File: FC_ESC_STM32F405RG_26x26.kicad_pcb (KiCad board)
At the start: 2 copper layers, 34 x 34 mm, 225 parts, among them J1 Conn_02x02_Odd_Even, J10 UART4, J11 PWM, J12 Conn_02x02_Odd_Even, J13 ALARM, J14 LED_STRIP, J15 RC, J16 MOTOR, J17 MOTOR, J18 MOTOR, J19 MOTOR, J2 ESC_PROG, J20 USB_A, J21 Conn_02x03_Odd_Even, J22 Conn_02x02_Odd_Even, J3 Debugger, J4 VOL_CUR, J5 RSSI, J6 I2C2_UART3, J7 SD CARD, J8 UART1, J9 UART6, Q1 SIZ200, Q10 SIZ200, Q11 SIZ200, Q12 SIZ200, Q2 SIZ200, Q3 SIZ200, Q4 SIZ200, Q5 SIZ200, Q6 SIZ200, Q7 SIZ200, Q8 SIZ200, Q9 SIZ200, U1 EFM8BB21, U10 FD6288Q, U11 outline, U12 MPU-6000, U13 BMP280, U15 STM32F405RGTx, U16 TPS54331D, U2 EFM8BB21, U3 TPS54560BDDA, U4 FD6288Q, U5 FD6288Q, U6 AT7456, U7 EFM8BB21, U8 EFM8BB21, U9 FD6288Q, Y1 8MHz, Y2 8Mhz

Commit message: update placement
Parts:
- removed J1, J22: Conn_02x02_Odd_Even, Proj_footprint:PinHeader_2x02_P1.27mm_Vertical_SMD
- removed J4: VOL_CUR, Connector_PinHeader_2.54mm:PinHeader_1x04_P2.54mm_Vertical
- added J23: ESC_PROG, Proj_footprint:ESC_Program, F.Cu at (199.2, 66.5)
- added J24: ESC_PROG, Proj_footprint:ESC_Program, F.Cu at (231.9, 66.5)
- added J25: ESC_PROG, Proj_footprint:ESC_Program, F.Cu at (199.2, 94.0)
- added R87: 2k2, Resistor_SMD:R_0402_1005Metric_Pad0.72x0.64mm_HandSolder, F.Cu at (225.1, 96.1)
- J2: value ESC_PROG -> Conn_02x04_Odd_Even; footprint Connector_PinHeader_2.54mm:PinHeader_1x09_P2.54mm_Vertical -> Proj_footprint:PinHeader_2x04_P1.27mm_Vertical_SMD
- J21: value Conn_02x03_Odd_Even -> ESC_PROG; footprint Connector_PinHeader_2.54mm:PinHeader_2x03_P2.54mm_Vertical -> Proj_footprint:ESC_Program
- J3: footprint Connector_PinHeader_2.54mm:PinHeader_1x04_P2.54mm_Vertical -> Proj_footprint:STLINK_Port
- moved J2 79.0 mm to (212.0, 94.8)
- moved J3 48.4 mm to (226.8, 96.6)
- moved J21 47.0 mm to (231.9, 94.0), turned to 90 degrees
- moved D18 1.10 mm to (201.2, 96.4)
- moved R80 1.07 mm to (203.8, 96.6)
- moved U12 0.56 mm to (218.0, 93.9)
- moved C22 0.38 mm to (211.2, 90.8)
- moved C16 0.23 mm to (210.8, 88.4)
- moved Q10 0.11 mm to (218.2, 65.6)
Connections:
- C22 pad 1: Net-(J1-Pin_3) -> Net-(J2-Pin_3)
- J2 pad 1: ESC1_C2CK -> 3V3_DEBUGGER
- J2 pad 2: ESC1_C2D -> Net-(J2-Pin_2)
- J2 pad 3: ESC2_C2CK -> Net-(J2-Pin_3)
- J2 pad 4: ESC2_C2D -> Net-(J2-Pin_2)
- J2 pad 5: ESC3_C2CK -> 3V3_FC
- J2 pad 6: ESC3_C2D -> Net-(J2-Pin_2)
- J2 pad 7: ESC4_C2CK -> 3V3_ESC
- J2 pad 8: ESC4_C2D -> Net-(J2-Pin_2)
- J21 pad 1: 3V3_FC -> ESC2_C2CK
- J21 pad 2: 3V3_FC -> ESC2_C2D
- J21 pad 3: STM32_BOOT0 -> GND
- L2 pad 2: Net-(J1-Pin_3) -> Net-(J2-Pin_3)
- R52 pad 1: Net-(J1-Pin_3) -> Net-(J2-Pin_3)
- U15 pad 28: STM32_BOOT1 -> unconnected-(U15-PB2-Pad28)
- U15 pad 60: STM32_BOOT0 -> 3V3_FC

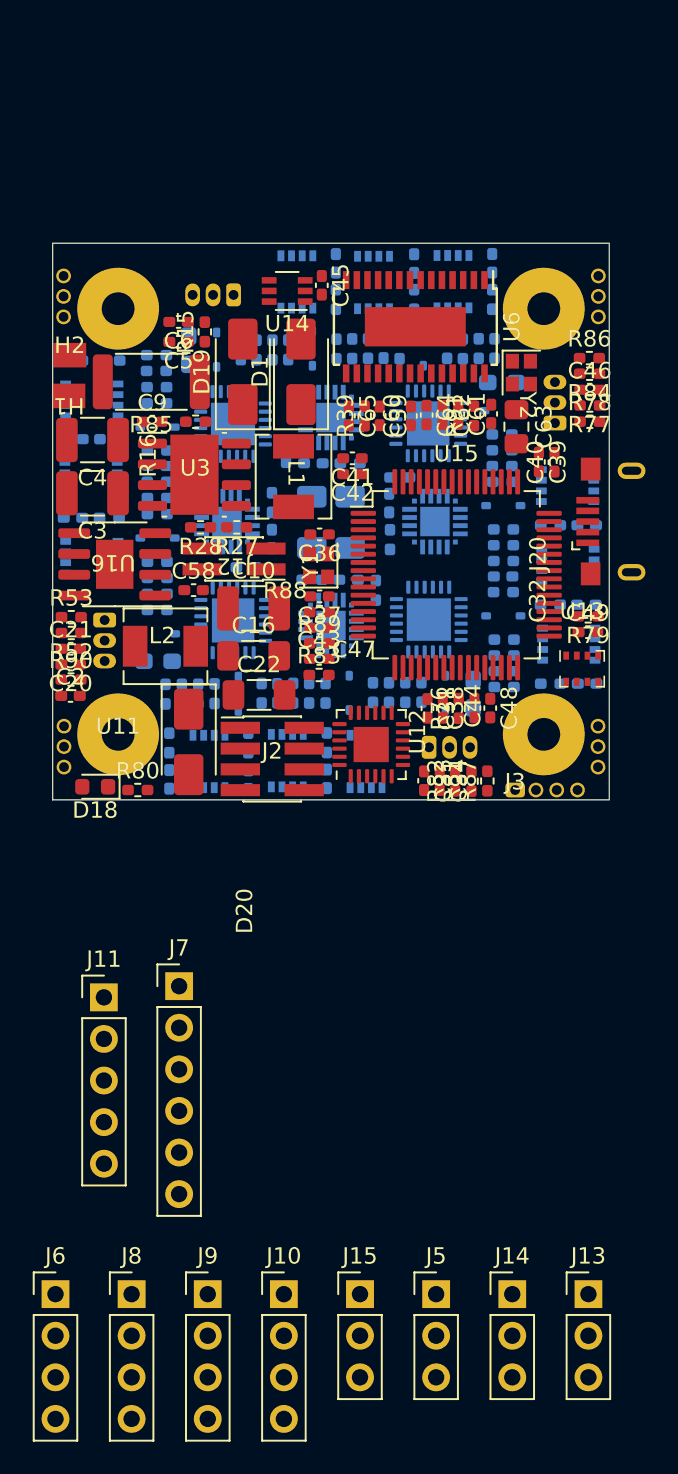
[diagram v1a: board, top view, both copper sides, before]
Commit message: update placement
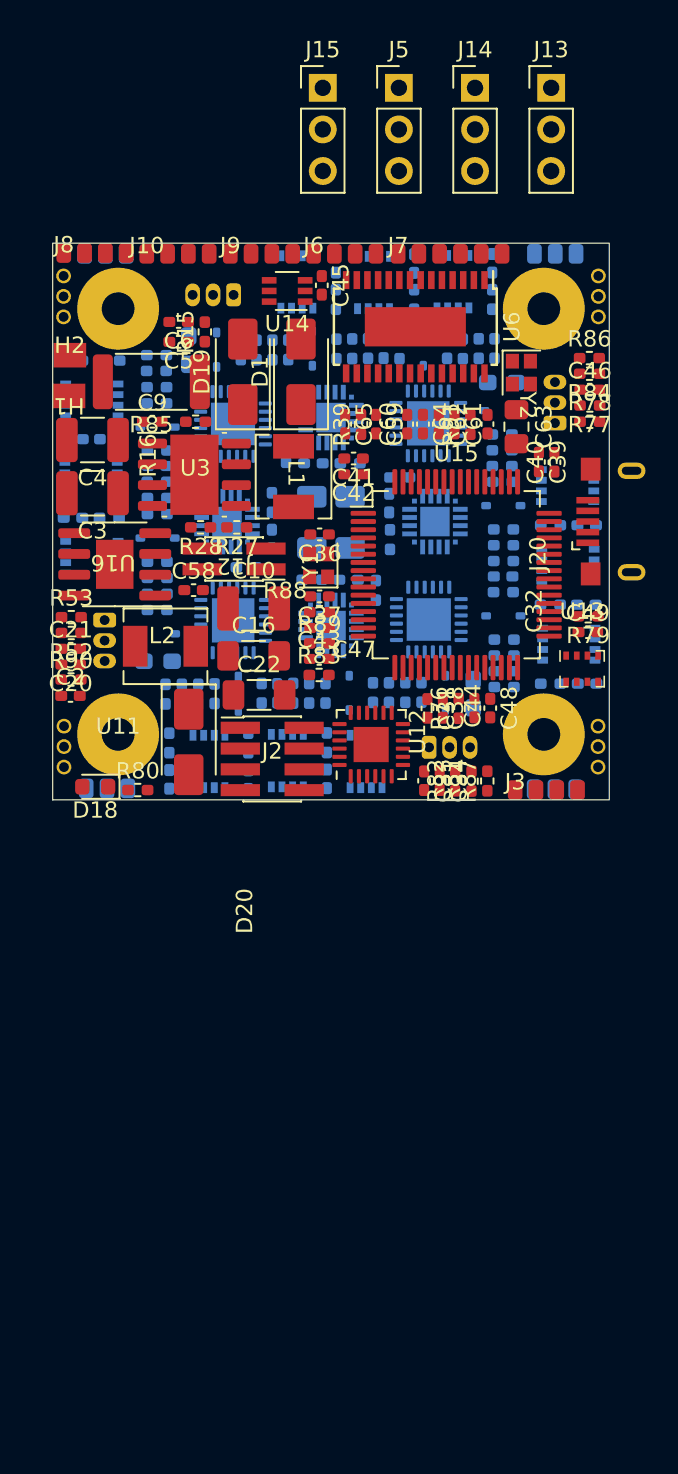
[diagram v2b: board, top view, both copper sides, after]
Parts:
- removed J11: PWM, Connector_PinHeader_2.54mm:PinHeader_1x05_P2.54mm_Vertical
- added J1: MOTOR, Proj_footprint:MountingPad_1x3, B.Cu at (228.0, 63.9)
- added J22: MOTOR, Proj_footprint:MountingPad_1x3, B.Cu at (203.1, 96.5)
- added J26: MOTOR, Proj_footprint:MountingPad_1x3, B.Cu at (203.0, 63.9)
- added J4: MOTOR, Proj_footprint:MountingPad_1x3, B.Cu at (228.0, 96.6)
- J10, J6, J8, J9: footprint Connector_PinHeader_2.54mm:PinHeader_1x04_P2.54mm_Vertical -> Proj_footprint:MoutingPad_1x4
- J3: footprint Proj_footprint:STLINK_Port -> Proj_footprint:MountingPad_1x4
- J7: footprint Connector_PinHeader_2.54mm:PinHeader_1x06_P2.54mm_Vertical -> Proj_footprint:MountingPad_1x6
- moved J13 73.7 mm to (229.0, 53.7)
- moved J14 73.7 mm to (224.4, 53.7)
- moved J15 73.7 mm to (215.1, 53.7)
- moved J5 73.7 mm to (219.7, 53.7)
- moved J6 65.5 mm to (214.5, 63.9)
- moved J10 64.1 mm to (204.3, 63.9)
- moved J8 63.7 mm to (199.2, 63.8)
- moved J9 63.6 mm to (209.4, 63.9)
- moved J7 46.7 mm to (219.7, 63.9)
- moved C32 0.66 mm to (225.1, 74.3)
- moved C61 0.64 mm to (223.1, 74.3)
- moved C62 0.60 mm to (222.1, 74.3)
- moved C64 0.60 mm to (221.2, 74.3)
- moved R39 0.57 mm to (217.4, 74.3)
- moved R91 0.57 mm to (224.1, 74.3)
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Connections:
- R81 pad 2: I2C2_SDA -> STM32_PB11
- R82 pad 2: I2C2_SCL -> STM32_PB10

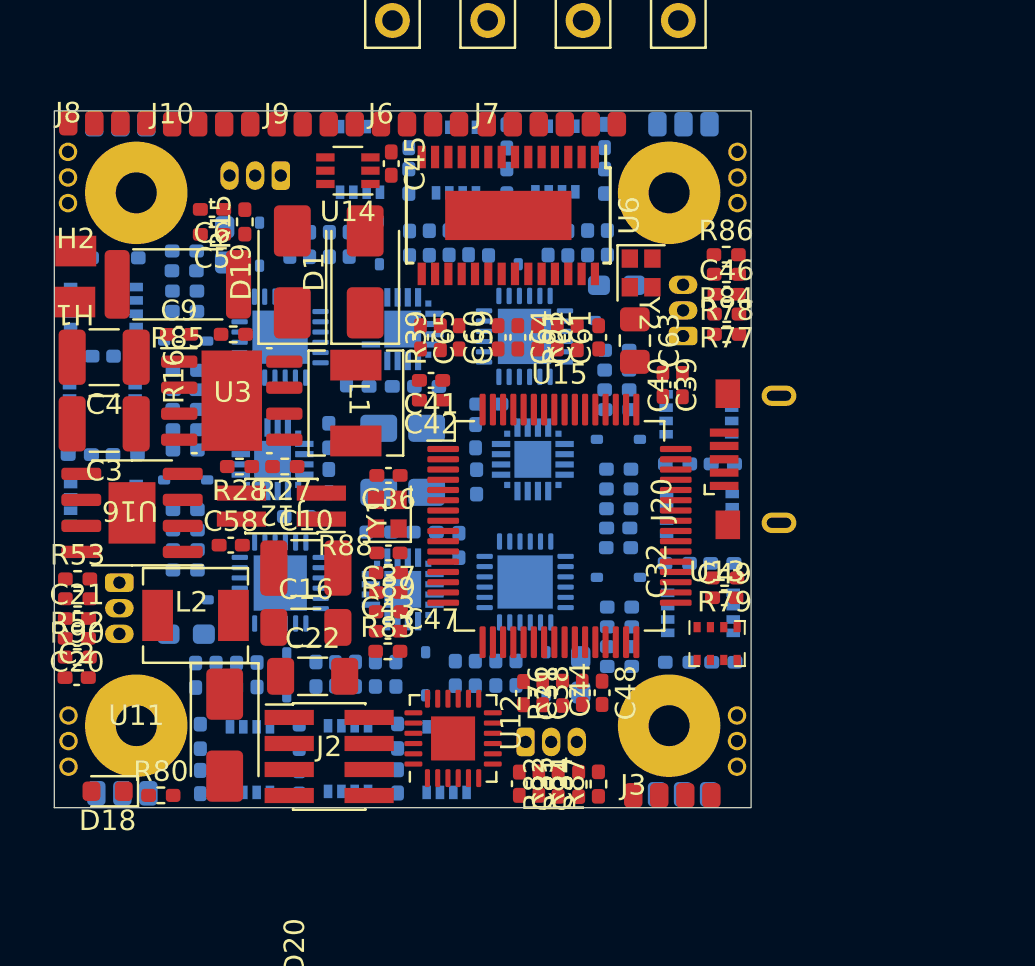
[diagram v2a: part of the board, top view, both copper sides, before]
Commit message: update placement
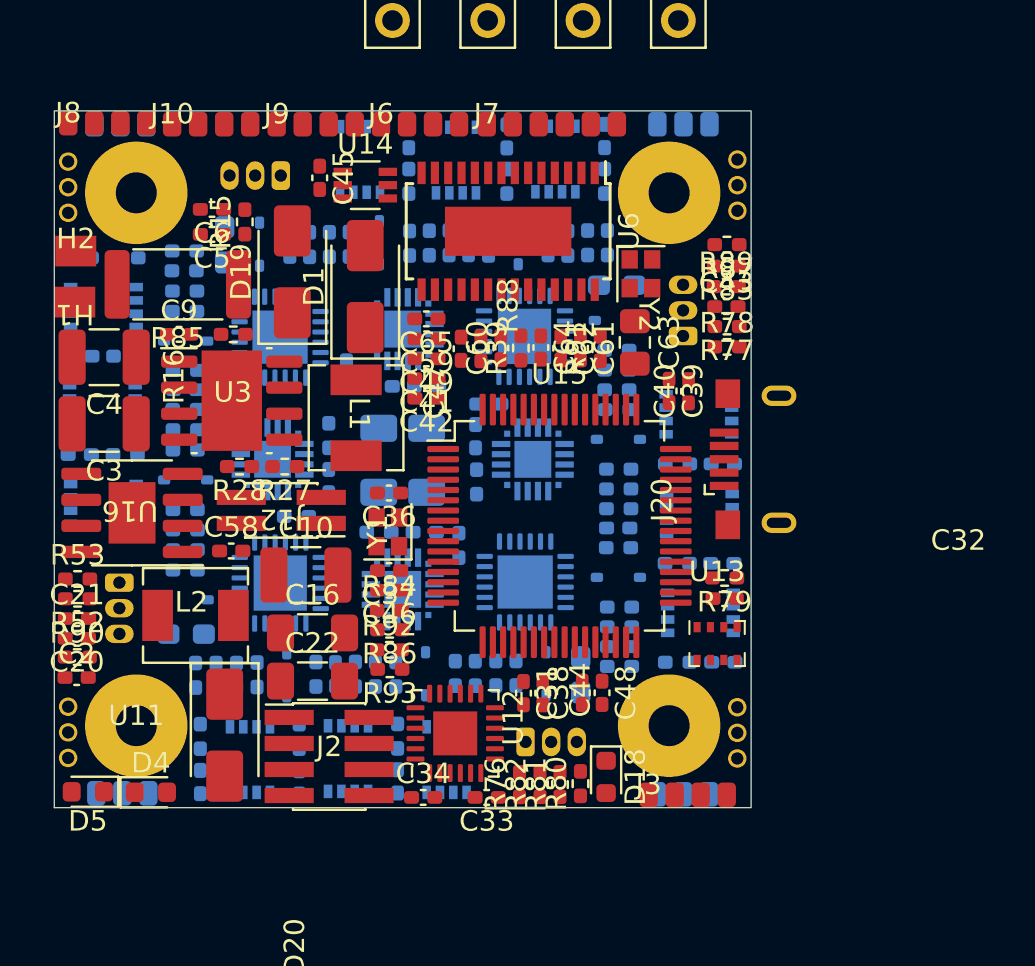
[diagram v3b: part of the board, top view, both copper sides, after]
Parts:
- added D4: LED_RED, LED_SMD:LED_0603_1608Metric, F.Cu at (203.3, 96.5)
- added D5: LED_RED, LED_SMD:LED_0603_1608Metric, F.Cu at (200.2, 96.5)
- added R92: 100R, Resistor_SMD:R_0402_1005Metric_Pad0.72x0.64mm_HandSolder, F.Cu at (214.9, 89.5)
- added R93: 100R, Resistor_SMD:R_0402_1005Metric_Pad0.72x0.64mm_HandSolder, F.Cu at (214.9, 90.5)
- moved R87 27.1 mm to (231.4, 69.8), turned to 180 degrees
- moved R83 25.0 mm to (231.3, 70.8), turned to 180 degrees
- moved R86 24.6 mm to (214.9, 88.6), turned to 180 degrees
- moved D18 24.3 mm to (225.5, 95.7), turned to -90 degrees
- moved R84 23.2 mm to (214.9, 87.6), turned to 0 degrees
- moved C43 22.9 mm to (231.3, 72.8)
- moved R89 22.9 mm to (231.3, 71.8)
- moved C46 21.9 mm to (214.9, 86.6), turned to 180 degrees
- moved R80 20.5 mm to (224.2, 96.1), turned to 90 degrees
- moved C49 18.6 mm to (216.7, 75.3), turned to 180 degrees
- moved C32 14.2 mm to (231.3, 87.0), turned to 0 degrees
- moved C47 12.4 mm to (218.4, 74.8), turned to 90 degrees
- moved R88 11.8 mm to (219.4, 74.8), turned to -90 degrees
- moved C34 5.68 mm to (216.6, 96.7), turned to 0 degrees
- moved R76 4.93 mm to (221.3, 96.1)
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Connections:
- net Net-(J12-Pin_3) renamed LED_PWR_5V
- net Net-(J2-Pin_2) renamed LED_PWR_3V3

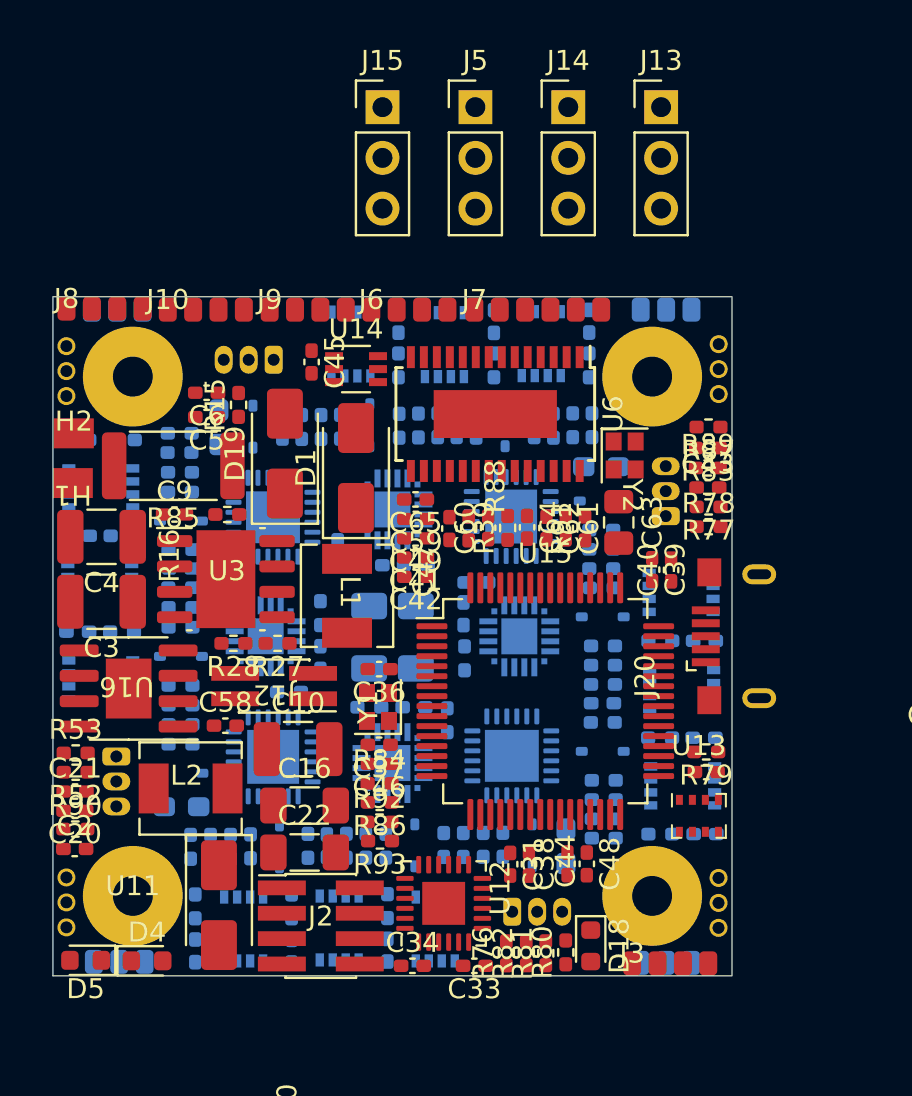
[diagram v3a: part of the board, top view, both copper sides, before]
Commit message: update placement
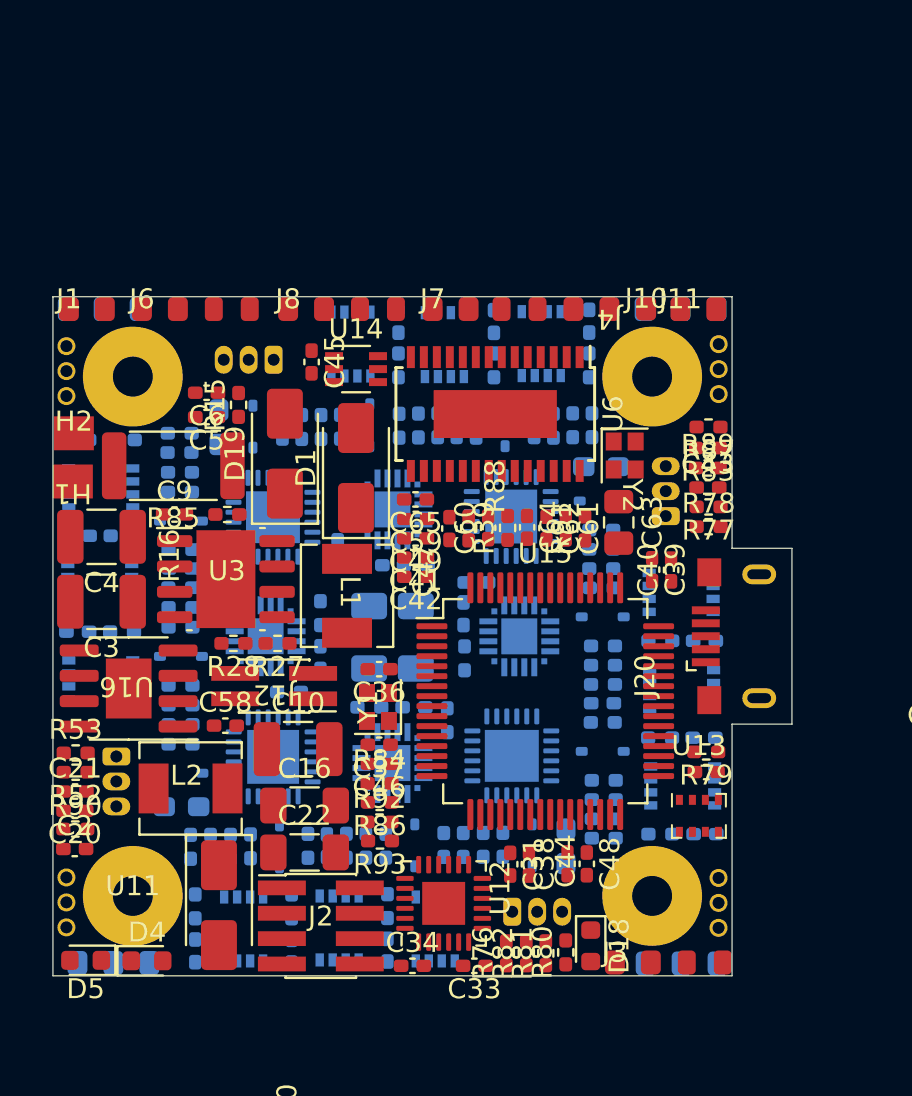
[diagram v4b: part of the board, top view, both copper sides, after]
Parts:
- removed J15: RC, Connector_PinHeader_2.54mm:PinHeader_1x03_P2.54mm_Vertical
- removed J22, J26: MOTOR, Proj_footprint:MountingPad_1x3
- added J11: Conn_01x02, Proj_footprint:MountingPad_1x2, F.Cu at (230.0, 63.8)
- J1: value MOTOR -> Conn_01x02; footprint Proj_footprint:MountingPad_1x3 -> Proj_footprint:MountingPad_5VOUT; moved to F.Cu
- J10: value UART4 -> Conn_01x01; footprint Proj_footprint:MoutingPad_1x4 -> Proj_footprint:MountingPad_1x1
- J13, J14, J5: footprint Connector_PinHeader_2.54mm:PinHeader_1x03_P2.54mm_Vertical -> Proj_footprint:MountingPad_1x3; moved to B.Cu
- J4: value MOTOR -> Conn_01x04; footprint Proj_footprint:MountingPad_1x3 -> Proj_footprint:MountingPad_1x4; moved to F.Cu
- J6: value I2C2_UART3 -> Conn_01x04; footprint Proj_footprint:MoutingPad_1x4 -> Proj_footprint:MountingPad_1x4
- J7: value SD CARD -> Conn_01x02; footprint Proj_footprint:MountingPad_1x6 -> Proj_footprint:MountingPad_5VOUT
- J8: value UART1 -> Conn_01x04; footprint Proj_footprint:MoutingPad_1x4 -> Proj_footprint:MountingPad_1x4
- J9: value UART6 -> LED_STRIP; footprint Proj_footprint:MoutingPad_1x4 -> Proj_footprint:MountingPad_1x3; moved to B.Cu
- moved J14 43.0 mm to (228.2, 96.6)
- moved J9 33.3 mm to (203.4, 96.6), turned to 180 degrees
- moved J4 32.8 mm to (226.4, 63.8), turned to 180 degrees
- moved J1 28.6 mm to (199.3, 63.8)
- moved J13 28.0 mm to (202.9, 63.8), turned to 180 degrees
- moved J10 24.0 mm to (228.3, 63.8)
- moved J5 13.2 mm to (228.2, 63.8)
- moved J6 11.5 mm to (203.0, 63.8)
- moved J8 11.1 mm to (210.3, 63.8)
- moved J7 2.09 mm to (217.6, 63.8)
- moved J3 0.87 mm to (226.7, 96.6)
- moved H1 0.08 mm to (199.5, 72.5)
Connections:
- J1 pad 1: +5V -> GND
- J1 pad 2: PWM5 -> +5V
- J10 pad 1: 3V3_FC -> RCIN_INT
- J4 pad 1: +5V -> SENS_RSSI
- J4 pad 2: PWM6 -> STM32_PA1
- J4 pad 3: GND -> STM32_PB10
- J6 pad 1: 3V3_FC -> SPI2_CS
- J6 pad 2: STM32_PB10 -> SPI2_MOSI
- J6 pad 3: STM32_PB11 -> SPI2_MISO
- J6 pad 4: GND -> SPI2_CLK
- J7 pad 1: 3V3_FC -> GND
- J7 pad 2: SPI2_CS -> +5V
- J8 pad 1: 3V3_FC -> UART6_TX
- J8 pad 2: UART1_RX -> UART6_RX
- J8 pad 3: UART1_TX -> UART1_RX
- J8 pad 4: GND -> UART1_TX
- J9 pad 1: 3V3_FC -> +5V
- J9 pad 2: UART6_TX -> PWM_OUT
- J9 pad 3: UART6_RX -> GND
- U15 pad 15: PWM5 -> STM32_PA1
- U15 pad 39: PWM7 -> PWM_OUT
- U15 pad 40: PWM8 -> unconnected-(U15-PC9-Pad40)
- U15 pad 41: PWM6 -> unconnected-(U15-PA8-Pad41)
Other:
- board size 34 x 34 mm -> 37 x 34 mm
